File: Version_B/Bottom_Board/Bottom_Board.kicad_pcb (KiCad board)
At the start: 2 copper layers, 74.8 x 84.5 mm, 57 parts, among them J1 Conn_02x03_Top_Bottom, J2 Conn_01x03_Pin, J3 Screw_Terminal_01x04, J4 DIN-5, J5 Conn_02x03_Top_Bottom, SW1 SW_DIP_x04, U1 LM324, U2 LM324, U3 ADS1015IDGSR

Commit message: minor fixe
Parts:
- R26, R27, R28, R29: value 10k -> 10K
- RV1, RV2: value 20K -> 20K POT
- U1, U2: value LM324 -> LM324DR

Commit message: aesthetic changes
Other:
- board text added: "VC1.05"
- board text removed: "VC1.04"
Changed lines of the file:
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@@
 			(drillshape 0)
 			(scaleselection 1)
-			(outputdirectory "Gerber/")
+			(outputdirectory "Manufacture/Gerber")
 		)
 	)
@@
 			(unlocked yes)
 			(layer "F.SilkS")
+			(hide yes)
 			(effects
 				(font
@@
 		(fp_arc
 			(start 1.499675 1.360299)
-			(mid 1.462521 1.447389)
+			(mid 1.462527 1.447384)
 			(end 1.375443 1.484532)
 			(stroke
@@
 		(fp_arc
 			(start 1.375443 -1.512619)
-			(mid 1.462507 -1.47545)
+			(mid 1.462521 -1.475453)
 			(end 1.499675 -1.388387)
 			(stroke
@@
 		(fp_arc
 			(start -1.373243 1.484531)
-			(mid -1.460292 1.447356)
+			(mid -1.460293 1.447356)
 			(end -1.49745 1.360299)
 			(stroke
@@
 		(tags "resistor")
 		(property "Reference" "R24"
-			(at -0.4704 -1.524 0)
+			(at -0.572 -1.524 0)
 			(layer "B.SilkS")
 			(effects
@@
 		(tags "resistor")
 		(property "Reference" "R23"
-			(at 2.2728 -0.254 0)
+			(at 2.2728 -0.2286 0)
 			(layer "B.SilkS")
 			(effects
@@
 		(tags "resistor")
 		(property "Reference" "R22"
-			(at 0.4704 -1.2202 0)
+			(at 0.5466 -1.2202 0)
 			(layer "B.SilkS")
 			(effects
@@
 		(tags "capacitor")
 		(property "Reference" "C6"
-			(at 0 1.016 0)
+			(at 0.0254 1.0668 0)
 			(layer "B.SilkS")
 			(effects
@@
 		)
 	)
-	(gr_text "VC1.04"
+	(gr_text "VC1.05"
 		(at 163.576 69.85 0)
 		(layer "F.SilkS")

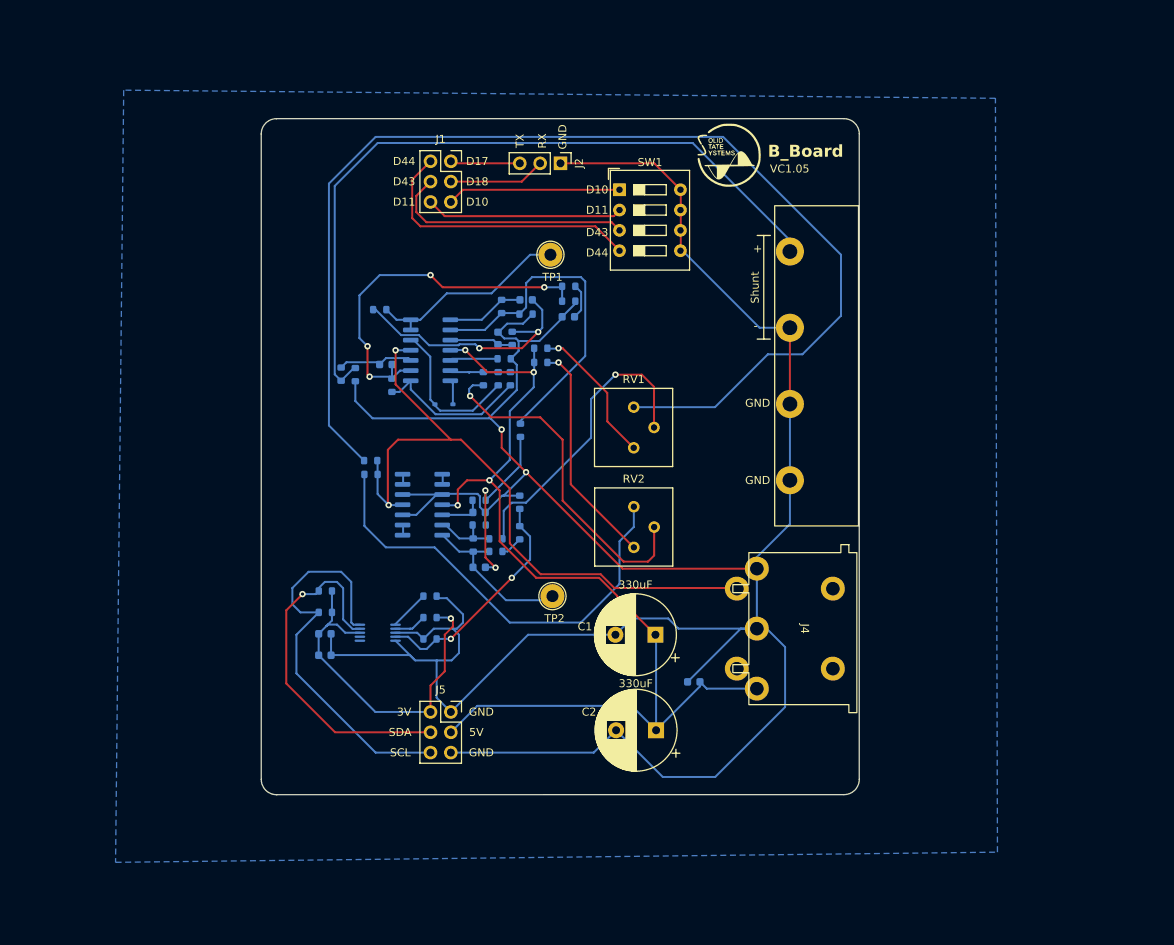
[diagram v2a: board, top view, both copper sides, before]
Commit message: fixed directory overwrite
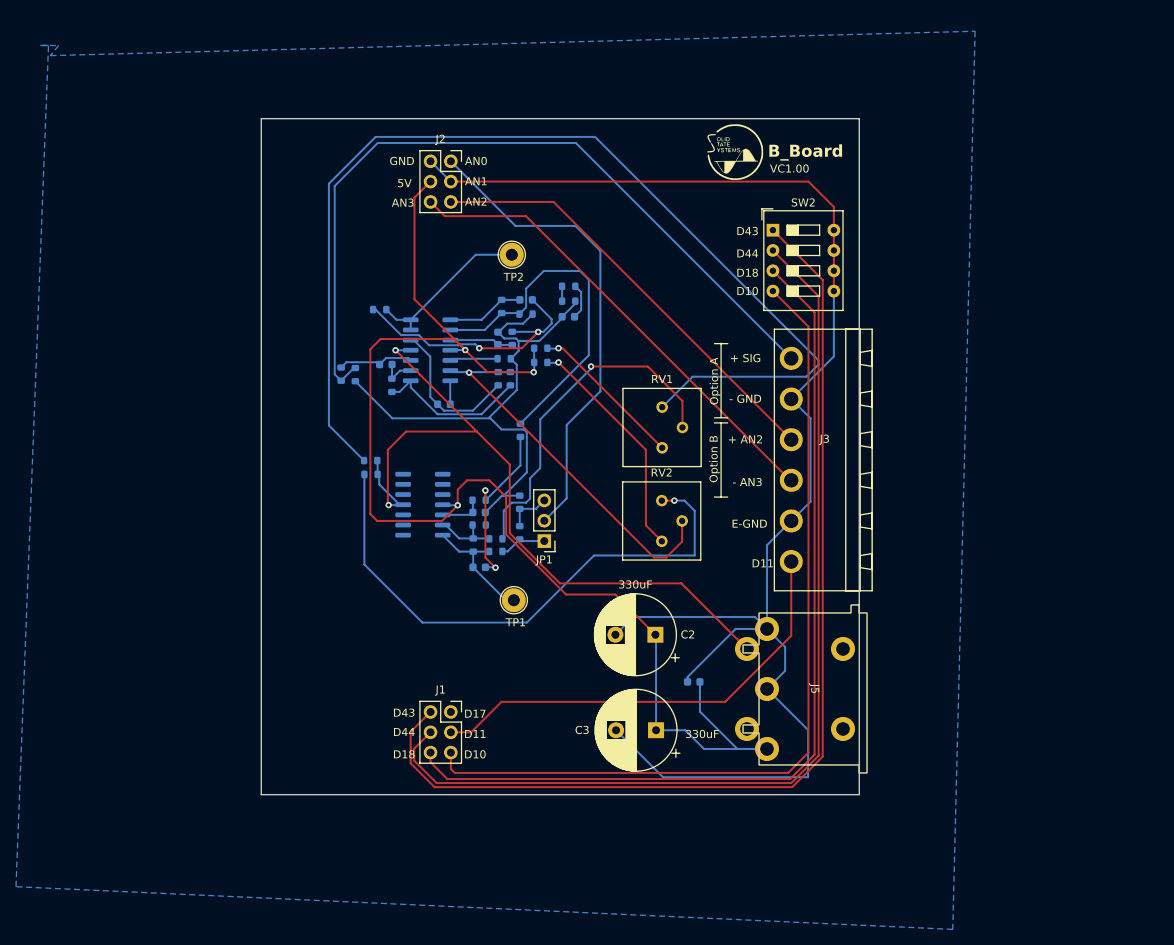
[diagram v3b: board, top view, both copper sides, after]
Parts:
- removed C10: 0.1uF, Capacitor_SMD:C_0603_1608Metric
- removed the C9 at (108.0, 127.4)
- removed the G*** at (158.5, 67.6)
- removed the G*** at (104.9, 67.1)
- removed the J2 at (137.4, 68.6)
- removed the R14 at (127.8, 95.5)
- removed R26, R27, R28, R29: 10K, Resistor_SMD:R_0603_1608Metric
- removed R30: 3.9M, Resistor_SMD:R_0603_1608Metric
- removed SW1: SW_DIP_x04, Button_Switch_THT:SW_DIP_SPSTx04_Slide_9.78x12.34mm_W7.62mm_P2.54mm
- removed U3: ADS1015IDGSR, bot_lib:DGS0010A_N
- added G***: LOGO, LOGO, F.Cu at (159.3, 67.2)
- added JP1: Jumper_3_Open, Connector_PinHeader_2.54mm:PinHeader_1x03_P2.54mm_Vertical, F.Cu at (135.4, 115.8)
- added SW2: SW_DIP_x04, Button_Switch_THT:SW_DIP_SPSTx04_Slide_9.78x12.34mm_W7.62mm_P2.54mm, F.Cu at (164.0, 76.9)
- C1: renamed from C11; value 0.1uF -> .1uF
- C5: renamed from C6; value 0.002uF -> .002uF
- C7: renamed from C4; value 0.1uF -> 0.1 uF
- C8: renamed from C3; value 0.1uF -> .1uF
- C9: renamed from C5; value 0.1uF -> .1uF
- D1: value 1N4148WS -> 1N914; footprint bot_lib:Diode_1N4148WS -> Diode_SMD:D_0603_1608Metric
- J1: renamed from J5; footprint bot_lib:PinSocket_2x03_P2.54mm_Vertical -> Connector_PinSocket_2.54mm:PinSocket_2x03_P2.54mm_Vertical
- J2: renamed from J1; footprint bot_lib:PinSocket_2x03_P2.54mm_Vertical -> Connector_PinSocket_2.54mm:PinSocket_2x03_P2.54mm_Vertical
- J3: value Screw_Terminal_01x04 -> Screw_Terminal_01x06; footprint bot_lib:Terminal_Strip_4_Pin -> Connector_Phoenix_MSTB:PhoenixContact_MSTBA_2,5_6-G-5,08_1x06_P5.08mm_Horizontal
- RV1, RV2: value 20K POT -> 20K; footprint bot_lib:Potentiometer_Bourns_3386P_Vertical -> Potentiometer_THT:Potentiometer_Bourns_3386P_Vertical
- U1, U2: value LM324DR -> LM324
- moved J3 10.2 mm to (166.3, 118.4)
- moved J5 7.65 mm to (169.2, 134.3)
- moved TP1 4.85 mm to (131.6, 123.2)
- moved TP2 4.83 mm to (131.3, 80.0)
- moved RV2 3.58 mm to (150.1, 115.8)
- moved RV1 3.56 mm to (150.1, 104.1)
- moved U2 0.06 mm to (120.2, 111.3)
- renumbered C1 to C2, C2 to C3, C8 to C4, C7 to C6, J4 to J5, R20 to R1, R1 to R10, R15 to R11, R24 to R12, R21 to R13, R19 to R14, R8 to R15, R12 to R16, R9 to R17, R13 to R19, R6 to R2, R5 to R20, R7 to R21, R16 to R22, R4 to R23, R3 to R24, R17 to R3, R10 to R4, R11 to R5, R22 to R6, R2 to R7, R25 to R8, R23 to R9, TP2 to TP1, TP1 to TP2
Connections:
- net +12V renamed 12V
- net Net-(R21-Pad2) renamed 2x_OUTPUT
- C1 pad 1: +5VD -> 5V
- C1 pad 2: GND -> AN1
- C2 pad 1: +5VD -> 5V
- C2 pad 2: GND -> AN1
- C3 pad 1: +5VD -> 5V
- C3 pad 2: GND -> AN1
- C6 pad 1: GND -> E60
- C7 pad 2: GND -> E60
- C9 pad 2: GND -> E60
- J1 pad 1: GND -> D17
- J1 pad 2: +3V0 -> D43
- J1 pad 3: +5VD -> D11
- J1 pad 4: SDA -> D44
- J1 pad 5: GND -> D10
- J1 pad 6: SCL -> D18
- J2 pad 1: TX -> AN0
- J2 pad 2: D44 -> AN1
- J2 pad 3: RX -> AN1
- J2 pad 4: D43 -> 5V
- J2 pad 5: D10 -> AN2
- J2 pad 6: D11 -> AN3
- J3 pad 1: GND -> D11
- J3 pad 2: GND -> AN1
- J3 pad 3: GND -> AN3
- J3 pad 4: E23_INPUT -> AN2
- J5 pad 1: GND -> AN1
- J5 pad 2: GND -> AN1
- J5 pad 3: +5VD -> 5V
- J5 pad 6: (no net) -> AN1
- J5 pad 7: (no net) -> AN1
- R10 pad 1: Net-(U1C--) -> Net-(R10-Pad1)
- R13 pad 1: AN0 -> 4x_OUTPUT
- R14 pad 1: GND -> E60
- R14 pad 2: AN0 -> 4x_OUTPUT
- R15 pad 1: +5VD -> 5V
- R17 pad 2: GND -> E60
- R2 pad 2: +5VD -> 5V
- R24 pad 2: GND -> E60
- R4 pad 2: GND -> E60
- R7 pad 1: Net-(U1C--) -> Net-(R10-Pad1)
- R7 pad 2: GND -> E60
- R9 pad 1: GND -> E60
- RV2 pad 2: Net-(R14-Pad2) -> Net-(U1B--)
- U1 pad 4: +5VD -> 5V
- U2 pad 1: Net-(U2A--) -> (no net)
- U2 pad 10: GND -> (no net)
- U2 pad 12: GND -> (no net)
- U2 pad 13: Net-(U2D--) -> (no net)
- U2 pad 14: Net-(U2D--) -> (no net)
- U2 pad 2: Net-(U2A--) -> (no net)
- U2 pad 3: GND -> (no net)
- U2 pad 4: +5VD -> 5V
- U2 pad 8: Net-(U2C--) -> (no net)
- U2 pad 9: Net-(U2C--) -> (no net)
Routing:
- net GND: track 366.4 -> 0.00 mm, vias 2 -> 0
- net AN1: track 0.00 -> 193.5 mm
- net 5V: track 0.00 -> 161.7 mm, vias 0 -> 3
- net +5VD: track 127.2 -> 0.00 mm, vias 4 -> 0
- net D18: track 0.00 -> 114.0 mm
- net D43: track 30.9 -> 130.2 mm
- net D44: track 35.7 -> 123.0 mm
- net D10: track 21.8 -> 107.5 mm
- net E60: track 0.00 -> 69.6 mm
- net AN3: track 0.00 -> 59.5 mm
- net AN2: track 0.00 -> 54.9 mm
- net SCL: track 50.4 -> 0.00 mm
- net SDA: track 45.3 -> 0.00 mm, vias 1 -> 0
- net +3V0: track 45.1 -> 0.00 mm, vias 1 -> 0
- net Net-(R14-Pad2): track 42.8 -> 0.00 mm, vias 1 -> 0
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- added copper zone on B.Cu, net AN1
- removed copper zone on B.Cu, net GND
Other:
- outline, holes or cut-outs redrawn
- board text added: "+ AN2"
- board text added: "+ SIG"
- board text added: "- AN3"
- board text added: "- GND"
- board text added: "AN0"
- board text added: "AN1"
- board text added: "AN2"
- board text added: "AN3"
- board text added: "E-GND"
- board text added: "Feather/LED Width"
- board text added: "Hardware Filter"
- board text added: "Option A"
- board text added: "Option B"
- board text added: "VC1.00"
- board text removed: "+"
- board text removed: "-"
- board text removed: "3V"
- board text removed: "RX"
- board text removed: "SCL"
- board text removed: "SDA"
- board text removed: "Shunt"
- board text removed: "TX"
- board text removed: "VC1.05"

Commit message: updated board b
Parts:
- C1, C8, C9: value .1uF -> 0.1uF
- C5: value .002uF -> 0.002uF
- C7: value 0.1 uF -> 0.1uF
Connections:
- J5 pad 6: AN1 -> (no net)
- J5 pad 7: AN1 -> (no net)
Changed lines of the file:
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@@
     (pad "5" thru_hole circle (at 5 8.5 270) (size 3 3) (drill 1.7) (layers "*.Cu" "*.Mask")
       (net 40 "12V") (pintype "passive"))
-    (pad "6" thru_hole circle (at -5 -3.5 270) (size 3 3) (drill 1.7) (layers "*.Cu" "*.Mask")
-      (net 3 "AN1"))
-    (pad "7" thru_hole circle (at 5 -3.5 270) (size 3 3) (drill 1.7) (layers "*.Cu" "*.Mask")
-      (net 3 "AN1"))
+    (pad "6" thru_hole circle (at -5 -3.5 270) (size 3 3) (drill 1.7) (layers "*.Cu" "*.Mask"))
+    (pad "7" thru_hole circle (at 5 -3.5 270) (size 3 3) (drill 1.7) (layers "*.Cu" "*.Mask"))
     (model "${KIPRJMOD}/Bottom_Board_3d/DIN_5_PIN.step"
       (offset (xyz 0 6.5 0))
@@
         (effects (font (size 1 1) (thickness 0.15)) (justify mirror))
     )
-    (fp_text value ".1uF" (at 1.425572 0.4125) (layer "B.Fab")
+    (fp_text value "0.1uF" (at 1.425572 0.4125) (layer "B.Fab")
         (effects (font (size 1 1) (thickness 0.15)) (justify mirror))
     )
@@
         (effects (font (size 1 1) (thickness 0.15)) (justify mirror))
     )
-    (fp_text value ".1uF" (at 0 -1.43) (layer "B.Fab")
+    (fp_text value "0.1uF" (at 0 -1.43) (layer "B.Fab")
         (effects (font (size 1 1) (thickness 0.15)) (justify mirror))
     )
@@
         (effects (font (size 1 1) (thickness 0.15)) (justify mirror))
     )
-    (fp_text value ".1uF" (at 1.956428 -4.064 90) (layer "B.Fab")
+    (fp_text value "0.1uF" (at 1.956428 -4.064 90) (layer "B.Fab")
         (effects (font (size 1 1) (thickness 0.15)) (justify mirror))
     )
@@
         (effects (font (size 1 1) (thickness 0.15)) (justify mirror))
     )
-    (fp_text value "0.1 uF" (at -0.0474 -1.3909) (layer "B.Fab")
+    (fp_text value "0.1uF" (at -0.0474 -1.3909) (layer "B.Fab")
         (effects (font (size 1 1) (thickness 0.15)) (justify mirror))
     )
@@
         (effects (font (size 1 1) (thickness 0.15)) (justify mirror))
     )
-    (fp_text value ".002uF" (at -4.060953 0) (layer "B.Fab")
+    (fp_text value "0.002uF" (at -4.060953 0) (layer "B.Fab")
         (effects (font (size 1 1) (thickness 0.15)) (justify mirror))
     )

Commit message: updated simulation circuit and finalized hardware design?
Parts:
- added J4: Screw_Terminal_01x05, bot_lib:BarrierStrip_1x05_P8.26mm_3.25in_Vertical, F.Cu at (165.4, 77.5)
- added J6: Conn_01x02_Pin, Connector_PinSocket_2.54mm:PinSocket_1x02_P2.54mm_Vertical, F.Cu at (135.4, 133.6)
- added J7: Conn_01x02_Pin, Connector_PinSocket_2.54mm:PinSocket_1x02_P2.54mm_Vertical, F.Cu at (135.4, 129.0)
- added J8: Screw_Terminal_01x04, Connector_PinHeader_2.54mm:PinHeader_1x04_P2.54mm_Vertical, F.Cu at (139.1, 68.6)
- added R25: 1M, Resistor_SMD:R_0603_1608Metric, B.Cu at (127.8, 95.5)
- J3: value Screw_Terminal_01x06 -> Conn_01x02_Pin; footprint Connector_Phoenix_MSTB:PhoenixContact_MSTBA_2,5_6-G-5,08_1x06_P5.08mm_Horizontal -> Connector_PinSocket_2.54mm:PinSocket_1x02_P2.54mm_Vertical
- moved J3 36.8 mm to (135.4, 138.4), turned to -90 degrees
- moved SW2 19.8 mm to (144.8, 71.9)
- moved JP1 5.05 mm to (135.4, 110.7), turned to 0 degrees
- moved RV2 3.58 mm to (146.6, 116.6)
- moved RV1 3.56 mm to (146.6, 104.1)
- renumbered TP1 to TP2, TP2 to TP3
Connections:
- J3 pad 1: D11 -> AN1
- J3 pad 2: AN1 -> D10
- R10 pad 1: Net-(R10-Pad1) -> Net-(U1C--)
- R12 pad 1: 2x_OUTPUT -> 4x_OUTPUT
- R13 pad 1: 4x_OUTPUT -> 2x_OUTPUT
- R13 pad 2: 2x_OUTPUT -> 4x_OUTPUT
- R14 pad 2: 4x_OUTPUT -> 2x_OUTPUT
- R7 pad 1: Net-(R10-Pad1) -> Net-(U1C--)
- RV2 pad 2: Net-(U1B--) -> Net-(R25-Pad2)
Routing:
- net D10: track 107.5 -> 172.0 mm
- net D44: track 123.0 -> 176.3 mm
- net D43: track 130.2 -> 183.4 mm
- net D18: track 114.0 -> 167.1 mm
- net D11: track 56.8 -> 11.7 mm
- net Net-(R25-Pad2): track 0.00 -> 42.8 mm, vias 0 -> 1
- net Net-(U1C--): track 4.56 -> 47.1 mm, vias 0 -> 4
- net Net-(U1B--): track 47.2 -> 7.64 mm, vias 1 -> 0
- net Net-(R18-Pad1): track 69.3 -> 52.7 mm, vias 1 -> 0
- net AN1: track 193.5 -> 209.5 mm
- net AN0: track 60.0 -> 75.4 mm
- net Net-(R3-Pad2): track 133.9 -> 147.2 mm
- net D17: track 0.00 -> 12.5 mm
- net E23_INPUT: track 97.6 -> 90.2 mm
- net 5V: track 161.7 -> 167.8 mm
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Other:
- outline, holes or cut-outs redrawn
- board text added: "2x"
- board text added: "4x"
- board text added: "E- GND"
- board text added: "No Filter"
- board text removed: "E-GND"
- board text removed: "Option A"
- board text removed: "Option B"

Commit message: connected e60 ground and an1
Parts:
- renumbered TP3 to TP1
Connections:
- C6 pad 1: E60 -> AN1
- C7 pad 2: E60 -> AN1
- C9 pad 2: E60 -> AN1
- R14 pad 1: E60 -> AN1
- R17 pad 2: E60 -> AN1
- R24 pad 2: E60 -> AN1
- R4 pad 2: E60 -> AN1
- R7 pad 2: E60 -> AN1
- R9 pad 1: E60 -> AN1
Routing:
- net E60: track 69.5 -> 0.00 mm, vias 2 -> 0
- net AN1: track 209.5 -> 279.0 mm, vias 0 -> 2
